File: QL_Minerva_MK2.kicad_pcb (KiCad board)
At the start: 2 copper layers, 42.5 x 44.5 mm, 16 parts, among them J1 Conn_01x02_Pin, J2 Conn_01x05_Pin, U1 Socket to QL, U2 W27C512, U3 PCB8563, U4 GAL16V8, U5 74LS133, Y1 Crystal

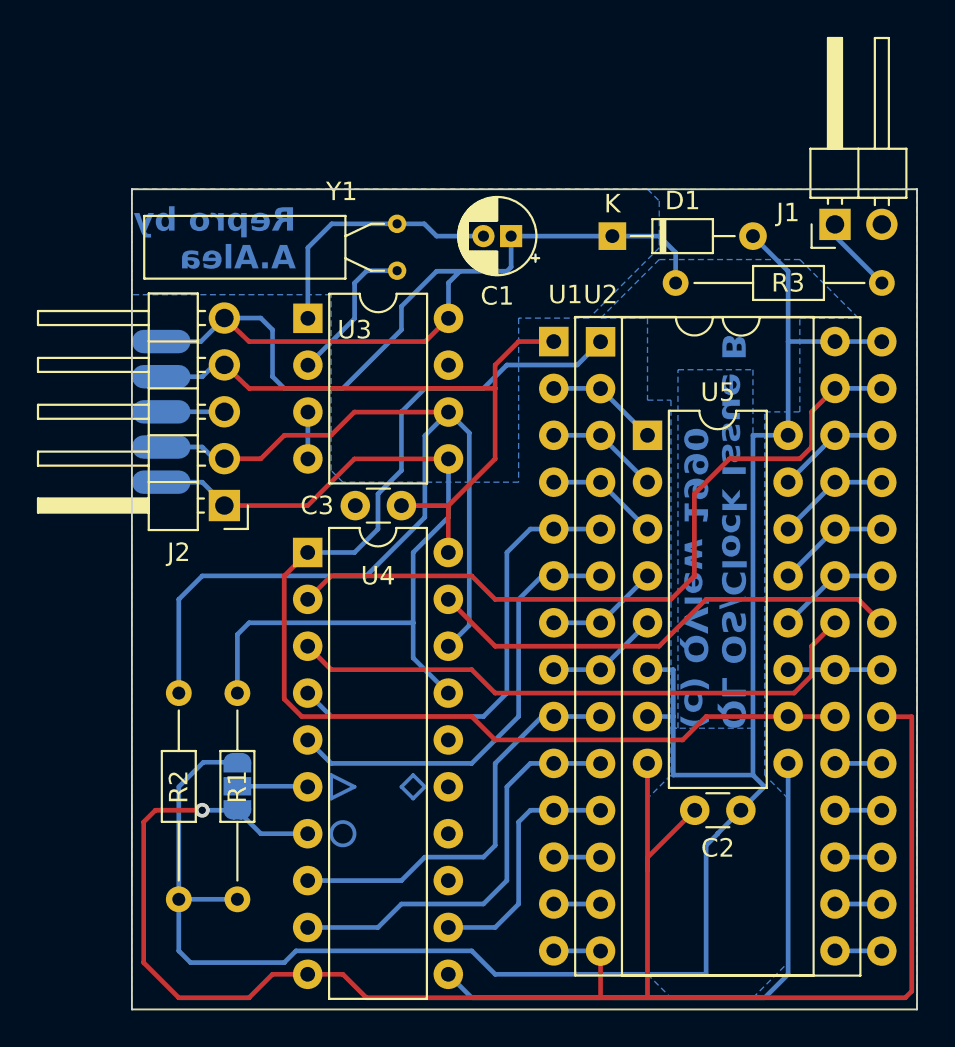
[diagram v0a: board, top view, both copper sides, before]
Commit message: update pin 6 of GAL
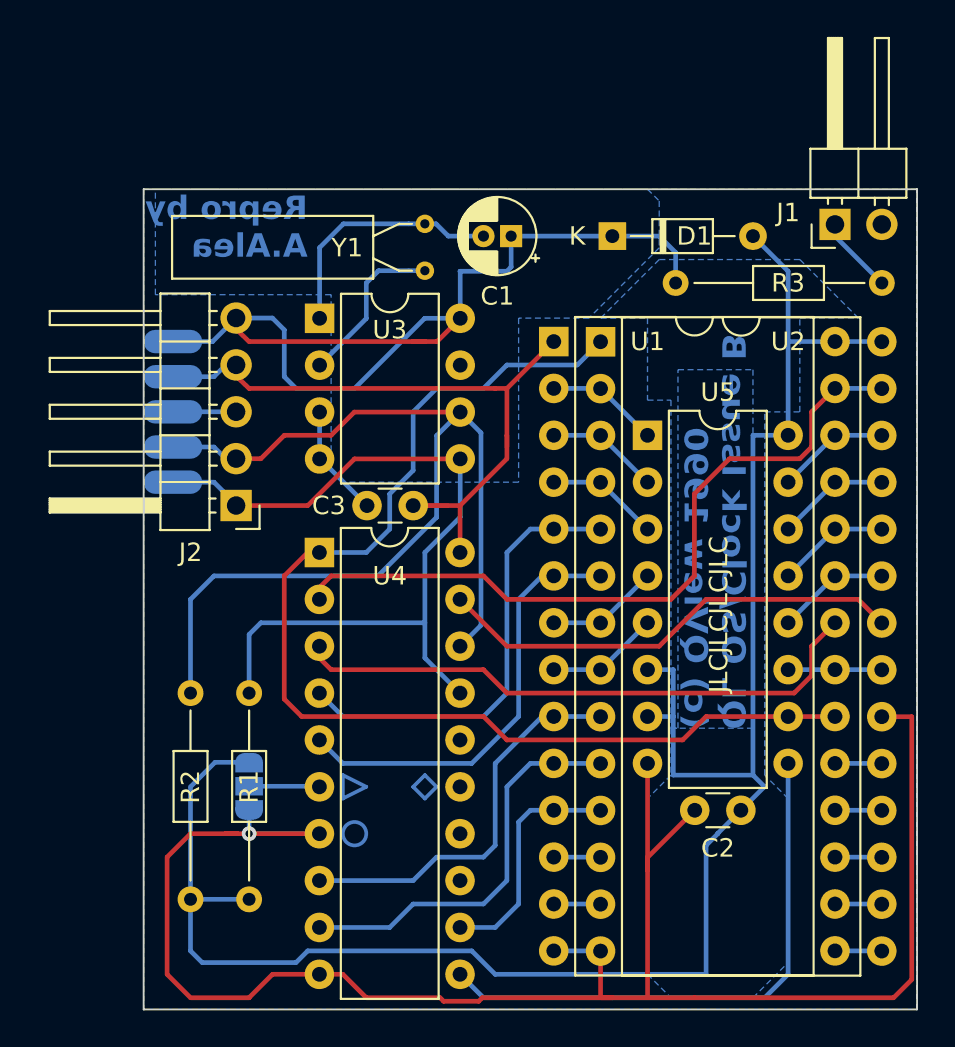
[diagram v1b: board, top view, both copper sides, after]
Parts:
- moved Y1 1.50 mm to (72.4, 58.4)
- moved JP1 0.64 mm to (62.9, 88.9)
- moved R1 0.64 mm to (62.9, 91.4)
- moved U3 0.64 mm to (66.7, 63.5)
- moved J2 0.63 mm to (62.2, 73.7)
- moved R2 0.63 mm to (59.7, 91.4)
- moved C3 0.63 mm to (71.8, 73.7)
- moved U4 0.63 mm to (66.7, 76.2)
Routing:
- net GND: track 107.0 -> 112.5 mm
- net +5V: track 36.7 -> 39.1 mm
- net /K: track 55.6 -> 54.2 mm
- net Net-(U3-X2): track 8.08 -> 8.95 mm
- net /IC_ROMOE: track 26.1 -> 25.5 mm
- net /DECODE: track 30.9 -> 30.3 mm
- net /A15: track 63.3 -> 62.7 mm
- net Net-(U3-X1): track 14.2 -> 13.5 mm
- net /A4: track 23.7 -> 23.0 mm
- net /A1: track 21.5 -> 20.9 mm
- net VCC: track 107.6 -> 107.0 mm
- net /A5: track 25.1 -> 24.4 mm
- net /A0: track 22.5 -> 21.9 mm
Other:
- board size 42.5 x 44.5 mm -> 41.9 x 44.5 mm
- board text added: "JLCJLCJLCJLC"

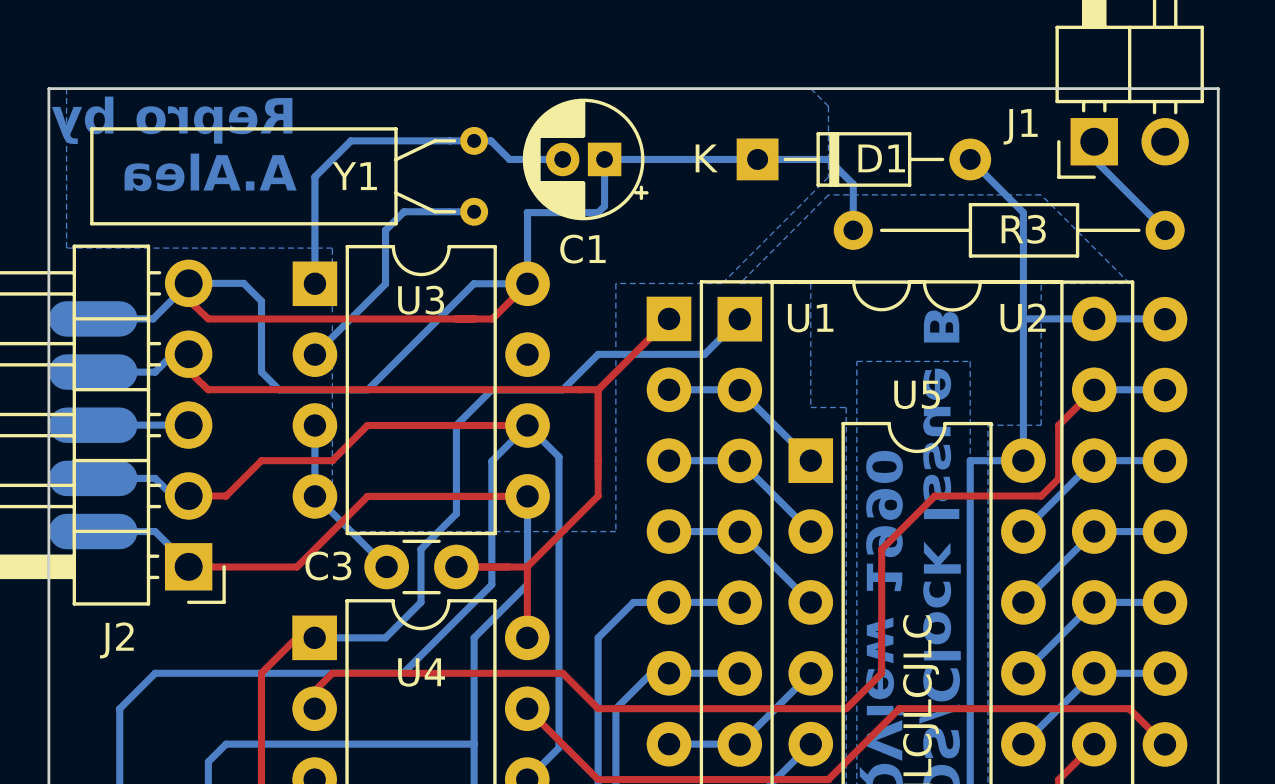
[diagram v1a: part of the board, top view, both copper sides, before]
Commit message: add values of components
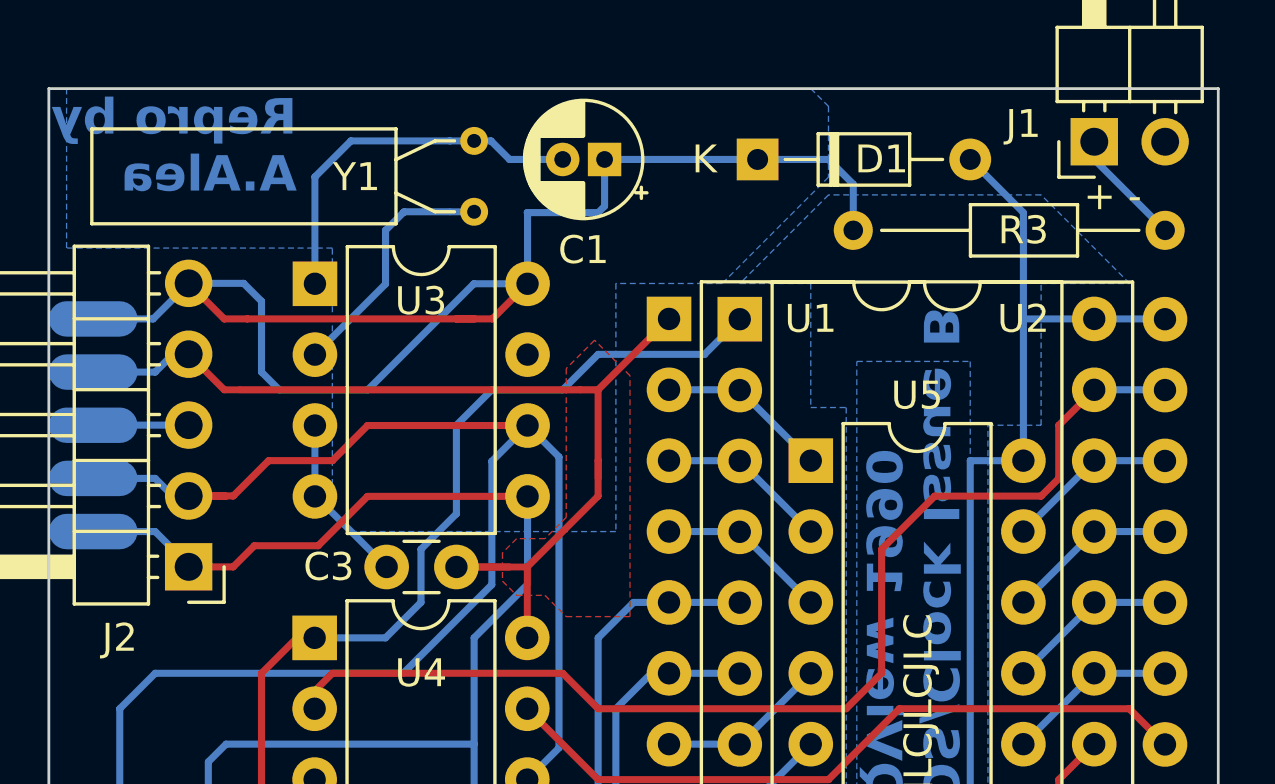
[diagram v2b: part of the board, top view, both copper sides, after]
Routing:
- net /SCL: track 57.9 -> 59.3 mm
- net /K: track 54.2 -> 53.6 mm
- net +5V: track 39.1 -> 38.5 mm
- added copper zone on F.Cu, net +5V
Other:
- board text added: "+ -"
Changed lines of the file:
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@@
+    (effects (font (size 1 1) (thickness 0.15)) (justify left bottom))
+  )
+  (gr_text "+ -" (at 94.234 60.96) (layer "F.SilkS")
     (effects (font (size 1 1) (thickness 0.15)) (justify left bottom))
   )
@@
   (segment (start 66.675 91.44) (end 62.865 91.44) (width 0.25) (layer "B.Cu") (net 3))
   (segment (start 66.685 71.13) (end 66.685 68.59) (width 0.254) (layer "B.Cu") (net 3))
-  (segment (start 64.77 69.85) (end 67.31 69.85) (width 0.254) (layer "F.Cu") (net 4))
   (segment (start 68.57 68.59) (end 73.67 68.59) (width 0.254) (layer "F.Cu") (net 4))
+  (segment (start 65.024 69.85) (end 67.31 69.85) (width 0.254) (layer "F.Cu") (net 4))
   (segment (start 67.31 69.85) (end 68.57 68.59) (width 0.254) (layer "F.Cu") (net 4))
+  (segment (start 63.759 71.115) (end 65.024 69.85) (width 0.254) (layer "F.Cu") (net 4))
+  (segment (start 62.16 71.115) (end 63.759 71.115) (width 0.254) (layer "F.Cu") (net 4))
   (segment (start 61.525 71.115) (end 63.5 71.12) (width 0.254) (layer "F.Cu") (net 4))
-  (segment (start 63.5 71.12) (end 64.77 69.85) (width 0.254) (layer "F.Cu") (net 4))
   (segment (start 69.85 77.47) (end 73.025 74.295) (width 0.254) (layer "B.Cu") (net 4))
   (segment (start 59.69 78.74) (end 60.96 77.47) (width 0.254) (layer "B.Cu") (net 4))
@@
   (segment (start 75.432 69.717) (end 75.432 80.143) (width 0.254) (layer "B.Cu") (net 4))
   (segment (start 73.025 74.295) (end 73.025 69.87) (width 0.254) (layer "B.Cu") (net 4))
-  (segment (start 66.04 73.66) (end 68.57 71.13) (width 0.254) (layer "F.Cu") (net 5))
-  (segment (start 61.525 73.655) (end 66.04 73.66) (width 0.254) (layer "F.Cu") (net 5))
+  (segment (start 68.57 71.13) (end 66.802 72.898) (width 0.254) (layer "F.Cu") (net 5))
+  (segment (start 64.513469 72.898) (end 63.754 73.657469) (width 0.254) (layer "F.Cu") (net 5))
+  (segment (start 63.754 73.657469) (end 61.525 73.655) (width 0.254) (layer "F.Cu") (net 5))
   (segment (start 73.67 71.13) (end 68.57 71.13) (width 0.254) (layer "F.Cu") (net 5))
+  (segment (start 66.802 72.898) (end 64.513469 72.898) (width 0.254) (layer "F.Cu") (net 5))
   (segment (start 59.69 72.39) (end 57.785 72.39) (width 1.27) (layer "B.Cu") (net 5))
   (segment (start 72.39 76.2) (end 74.305 74.285) (width 0.254) (layer "B.Cu") (net 5))
@@
   (segment (start 94.615 67.31) (end 97.14 67.31) (width 0.254) (layer "B.Cu") (net 40))
   (segment (start 72.41 64.77) (end 71.755 64.77) (width 0.254) (layer "F.Cu") (net 41))
-  (segment (start 71.755 64.77) (end 62.865 64.77) (width 0.254) (layer "F.Cu") (net 41))
-  (segment (start 62.865 64.77) (end 61.525 63.495) (width 0.254) (layer "F.Cu") (net 41))
+  (segment (start 63.435 64.77) (end 64.262 64.77) (width 0.254) (layer "F.Cu") (net 41))
   (segment (start 74.305 63.51) (end 73.045 64.77) (width 0.254) (layer "F.Cu") (net 41))
   (segment (start 73.045 64.77) (end 71.755 64.77) (width 0.254) (layer "F.Cu") (net 41))
+  (segment (start 62.16 63.495) (end 63.435 64.77) (width 0.254) (layer "F.Cu") (net 41))
+  (segment (start 71.755 64.77) (end 64.262 64.77) (width 0.254) (layer "F.Cu") (net 41))
   (segment (start 60.885 64.77) (end 62.16 63.495) (width 0.254) (layer "B.Cu") (net 41))
   (segment (start 64.77 66.675) (end 64.77 64.135) (width 0.254) (layer "B.Cu") (net 41))
@@
   (segment (start 85.09 59.055) (end 82.55 59.055) (width 0.254) (layer "B.Cu") (net 41))
   (segment (start 79.375 64.77) (end 76.835 67.31) (width 0.254) (layer "F.Cu") (net 42))
+  (segment (start 62.16 66.035) (end 63.435 67.31) (width 0.25) (layer "F.Cu") (net 42))
   (segment (start 76.835 69.85) (end 76.835 70.485) (width 0.254) (layer "F.Cu") (net 42))
-  (segment (start 62.865 67.31) (end 76.2 67.31) (width 0.254) (layer "F.Cu") (net 42))
+  (segment (start 63.435 67.31) (end 64.008 67.31) (width 0.25) (layer "F.Cu") (net 42))
   (segment (start 76.835 67.31) (end 76.835 69.85) (width 0.254) (layer "F.Cu") (net 42))
   (segment (start 74.295 73.66) (end 76.835 71.12) (width 0.25) (layer "F.Cu") (net 42))
@@
   (segment (start 71.12 73.66) (end 73.66 73.66) (width 0.254) (layer "F.Cu") (net 42))
   (segment (start 76.835 67.31) (end 76.2 67.31) (width 0.254) (layer "F.Cu") (net 42))
+  (segment (start 64.008 67.31) (end 76.2 67.31) (width 0.254) (layer "F.Cu") (net 42))
   (segment (start 71.755 73.66) (end 74.295 73.66) (width 0.25) (layer "F.Cu") (net 42))
   (segment (start 74.295 76.2) (end 74.295 73.66) (width 0.25) (layer "F.Cu") (net 42))
-  (segment (start 61.525 66.035) (end 62.865 67.31) (width 0.254) (layer "F.Cu") (net 42))
   (segment (start 59.69 66.675) (end 60.96 66.675) (width 0.254) (layer "B.Cu") (net 42))
   (segment (start 60.96 66.675) (end 61.6 66.035) (width 0.254) (layer "B.Cu") (net 42))
   (segment (start 59.69 66.675) (end 57.785 66.675) (width 1.27) (layer "B.Cu") (net 42))
+  (zone (net 42) (net_name "+5V") (layer "F.Cu") (hatch edge 0.5)
+    (priority 3)
+    (connect_pads (clearance 0.5))
+    (min_thickness 0.25) (filled_areas_thickness no)
+    (fill yes (thermal_gap 0.5) (thermal_bridge_width 0.5))
+    (polygon
+      (pts
+        (xy 73.914 74.676)
+        (xy 74.93 74.676)
+        (xy 75.692 75.438)
+        (xy 77.978 75.438)
+        (xy 77.978 66.802)
+        (xy 76.708 65.532)
+        (xy 75.692 66.548)
+        (xy 75.692 71.882)
+        (xy 74.93 72.644)
+        (xy 73.914 72.644)
+        (xy 73.406 73.152)
+        (xy 73.406 74.168)
+      )
+    )
+  )
   (zone (net 3) (net_name "GND") (layer "F.Cu") (hatch edge 0.5)
     (priority 2)

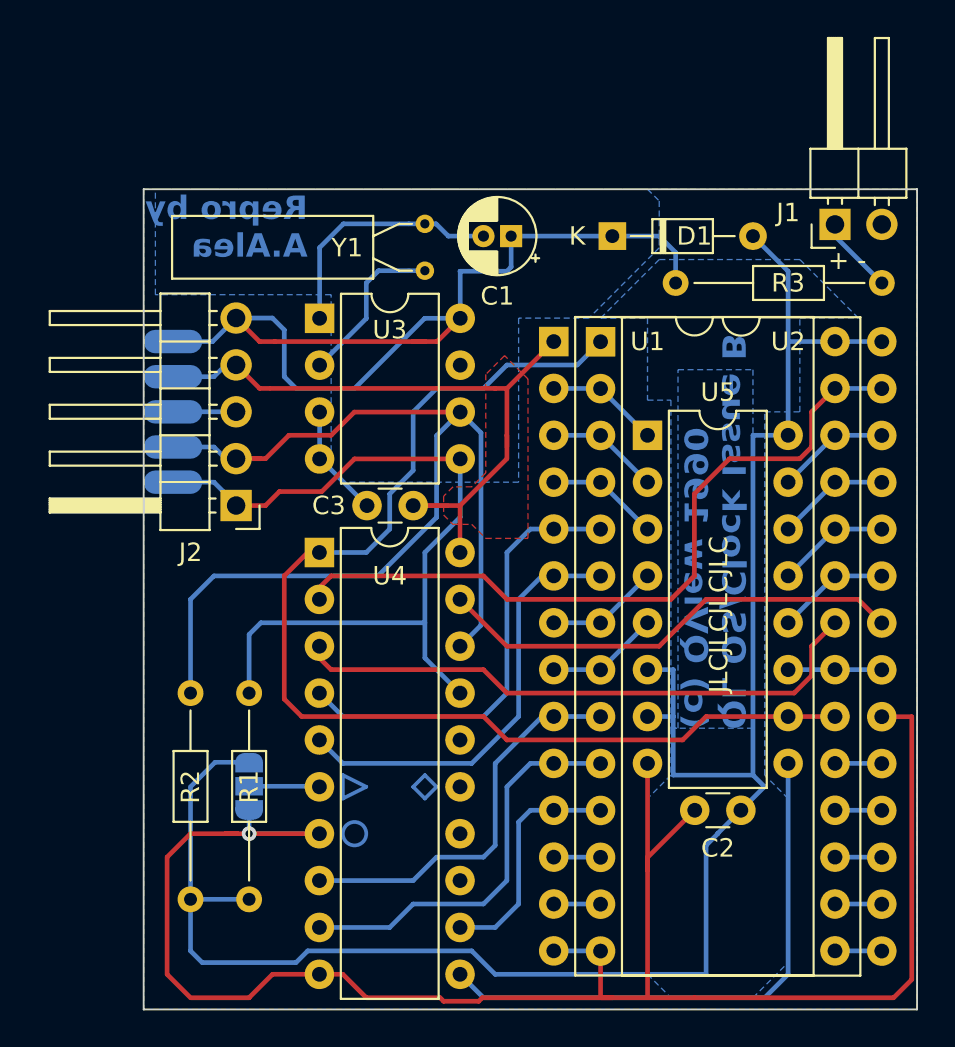
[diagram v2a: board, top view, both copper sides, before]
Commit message: Fix references
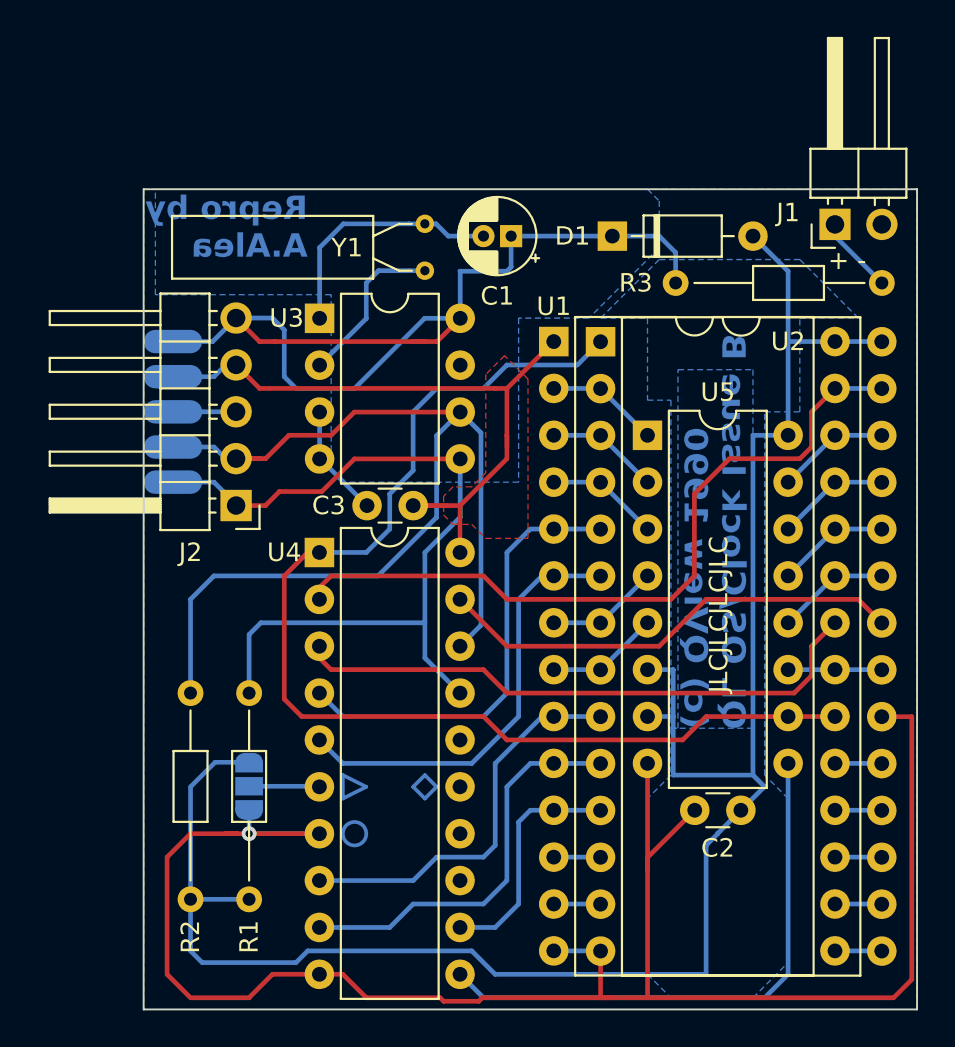
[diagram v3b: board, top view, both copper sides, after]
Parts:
- C1: value C_Variable -> 30p Variable
- D1: value D_Zener -> BAT42; footprint Diode_THT:D_DO-34_SOD68_P7.62mm_Horizontal -> Diode_THT:D_DO-35_SOD27_P7.62mm_Horizontal
- R1, R2: value R -> 2K2
- R3: value R -> 120
- U3: value PCB8563 -> PCF8583P
- Y1: value Crystal -> 32.768 kHz
